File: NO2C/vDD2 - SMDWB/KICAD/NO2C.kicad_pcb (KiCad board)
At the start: 4 copper layers, 104.8 x 64 mm, 195 parts, among them IC1 TC4424AVOA, IC2 MPXH6400AC6T1, IC3 VNS3NV04DPTR-E, IC4 CONN_02X08, J1 3-6437285-0, J2 USB_C_Receptacle_USB2.0_16P, J3 Conn_02x03_Odd_Even, P1 Conn_01x04, P4 Conn_01x04, Q1 BSP78HUMA1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

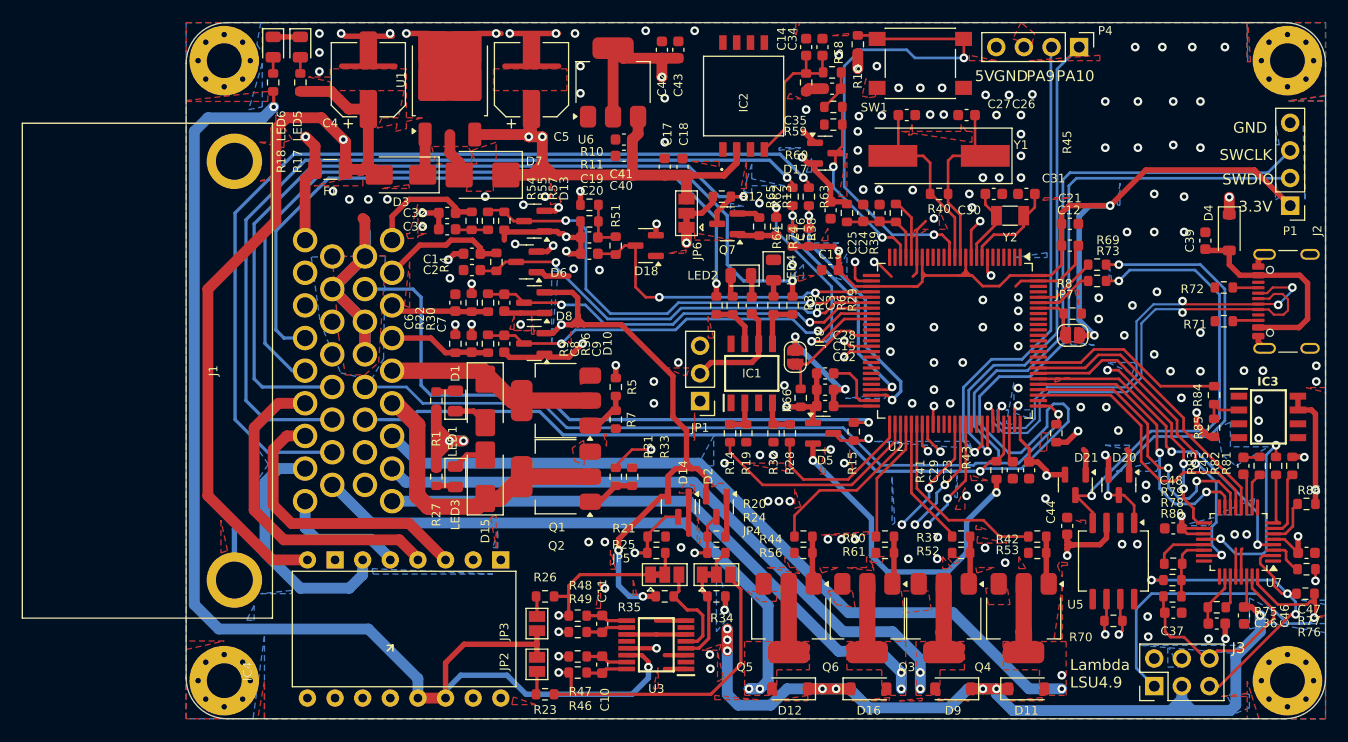
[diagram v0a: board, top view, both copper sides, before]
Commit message: plugin wideband
Added wide band to the main connector.
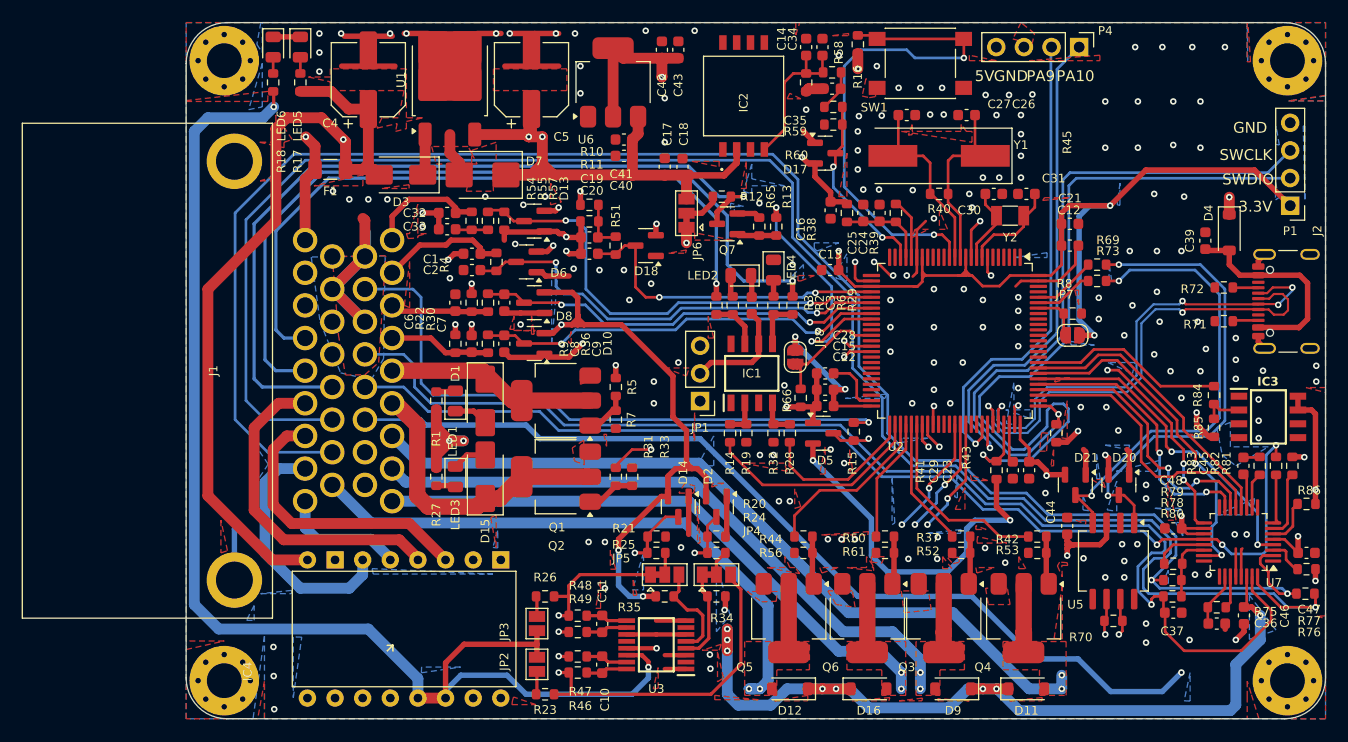
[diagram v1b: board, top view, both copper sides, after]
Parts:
- removed J3: Conn_02x03_Odd_Even, Connector_PinHeader_2.54mm:PinHeader_2x03_P2.54mm_Vertical
- removed R62, R63: 0R, Resistor_SMD:R_0603_1608Metric
- removed R64, R74: 10K, Resistor_SMD:R_0603_1608Metric
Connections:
- J1 pad 15: Net-(J1-Pad15) -> IP
- J1 pad 16: Net-(J1-Pad16) -> IA
- J1 pad 21: GND -> UN
- J1 pad 22: /SWCLK -> VM
- J1 pad 23: /SWDIO -> HEAT-
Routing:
- net IA: track 33.7 -> 167.2 mm, vias 3 -> 2
- net IP: track 38.0 -> 167.2 mm
- net UN: track 20.5 -> 111.2 mm, vias 0 -> 1
- net Net-(J1-Pad16): track 85.7 -> 0.00 mm, vias 1 -> 0
- net HEAT-: track 34.1 -> 119.5 mm, vias 1 -> 2
- net Net-(J1-Pad15): track 79.1 -> 0.00 mm, vias 1 -> 0
- net VM: track 32.1 -> 100.9 mm, vias 2 -> 3
- net /SWCLK: track 126.4 -> 63.4 mm
- net /SWDIO: track 135.3 -> 75.0 mm
- net /SDA: track 25.0 -> 0.00 mm, vias 2 -> 0
- net /SCL: track 23.6 -> 0.00 mm, vias 2 -> 0
- net GND: track 208.0 -> 197.1 mm, vias 167 -> 183
- net +12V: track 307.5 -> 302.1 mm
- net /SPI3_MISO: track 27.5 -> 25.8 mm
- net /PA9: track 45.5 -> 44.0 mm
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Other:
- board text added: "20241123"
- board text added: "HEAT"
- board text added: "R04"
- board text removed: "20241118"
- board text removed: "R03"
- board text removed: "SCL"
- board text removed: "SDA"
